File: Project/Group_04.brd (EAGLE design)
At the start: 71.4 x 57.1 mm, 29 parts, among them J1 POWER_JACKPTH_LOCK, U1 +12v

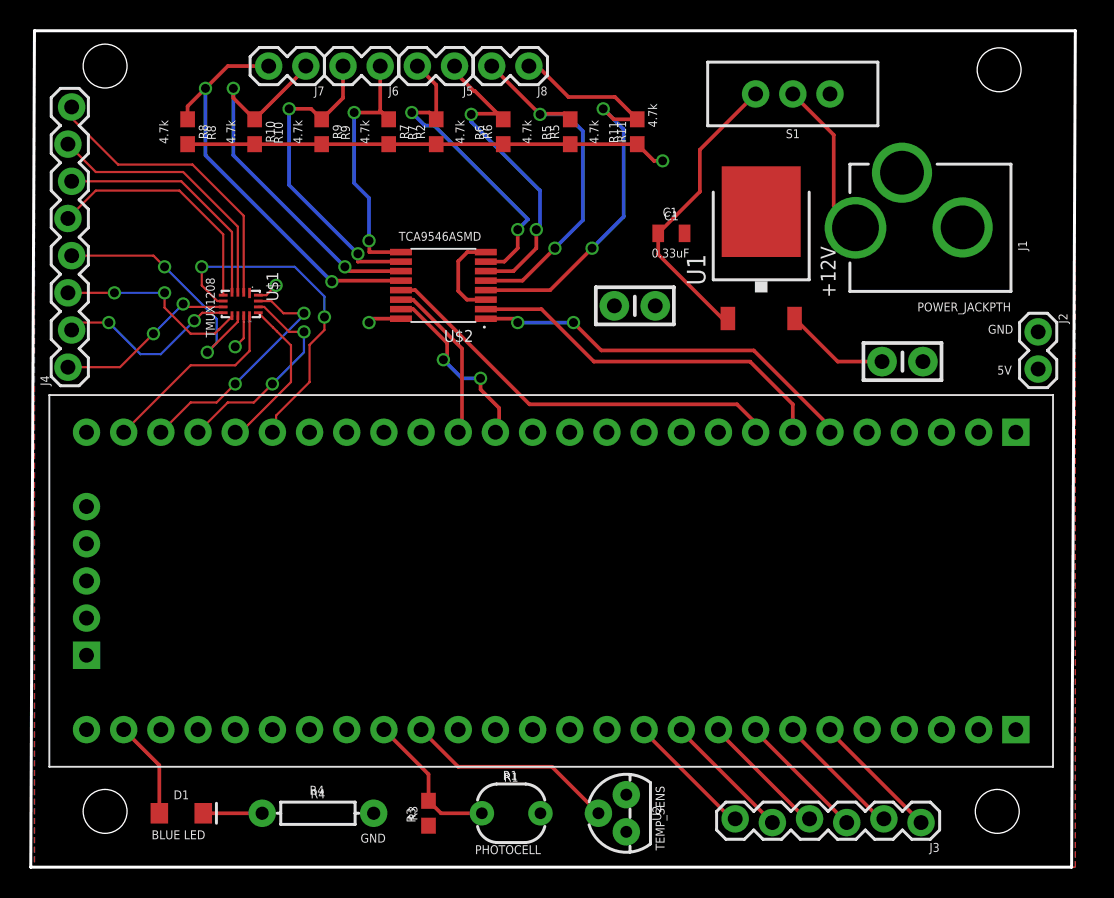
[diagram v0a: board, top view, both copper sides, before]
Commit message: fixed dimension
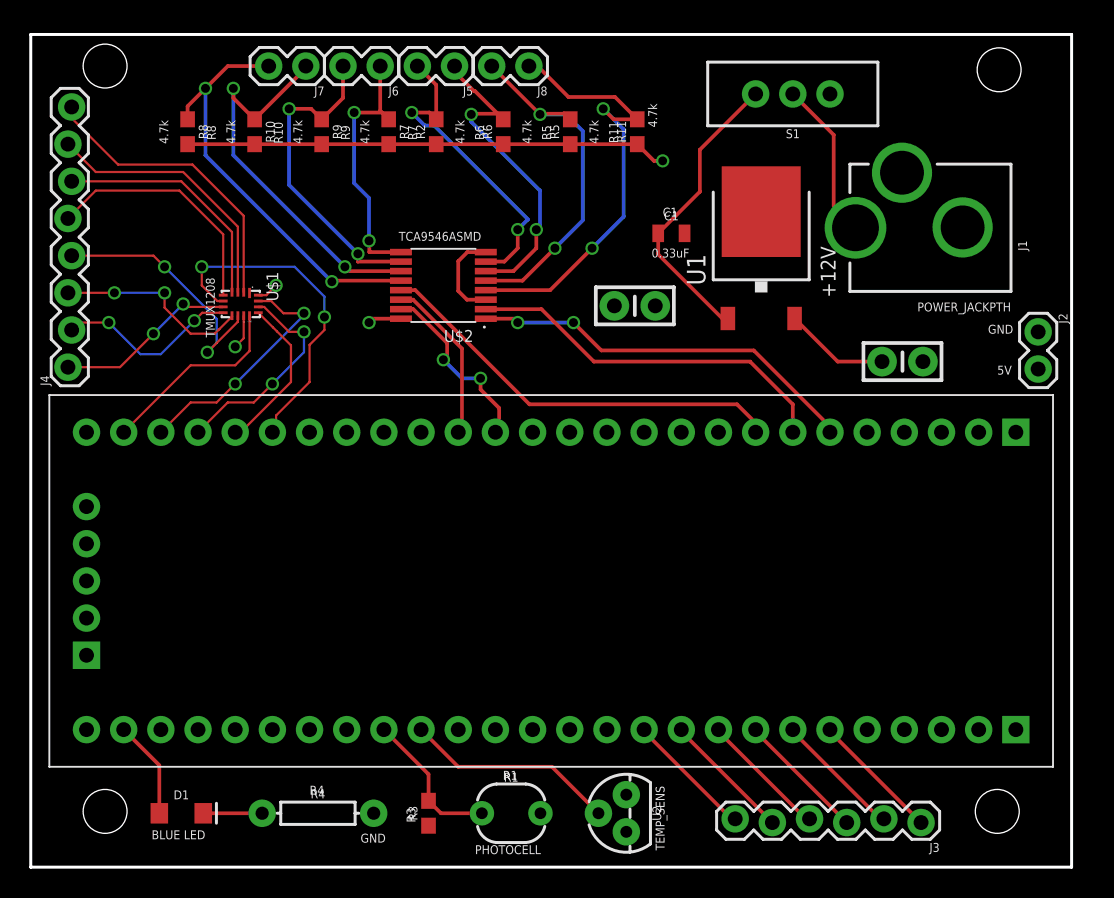
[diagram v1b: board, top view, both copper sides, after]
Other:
- board size 71.4 x 57.1 mm -> 71.1 x 56.9 mm
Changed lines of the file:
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@@
 <plain>
 <wire x1="0" y1="0" x2="71.12" y2="0" width="0.2032" layer="20"/>
-<wire x1="71.12" y1="0" x2="71.374" y2="57.15" width="0.2032" layer="20"/>
-<wire x1="71.374" y1="57.15" x2="0.254" y2="57.15" width="0.2032" layer="20"/>
-<wire x1="0.254" y1="57.15" x2="0" y2="0" width="0.2032" layer="20"/>
+<wire x1="71.12" y1="0" x2="71.12" y2="56.896" width="0.2032" layer="20"/>
+<wire x1="71.12" y1="56.896" x2="0" y2="56.896" width="0.2032" layer="20"/>
+<wire x1="0" y1="56.896" x2="0" y2="0" width="0.2032" layer="20"/>
 <hole x="5.08" y="3.81" drill="3"/>
 <hole x="66.04" y="3.81" drill="3"/>
@@
 <text x="14.478" y="37.211" size="0.1016" layer="21">5V</text>
 <dimension x1="0" y1="0" x2="71.12" y2="0" x3="35.56" y3="-3.81" textsize="1.778" layer="51" visible="yes"/>
-<dimension x1="0" y1="0" x2="0.254" y2="57.15" x3="-3.6829625" y3="28.59193125" textsize="1.778" layer="51" visible="yes"/>
+<dimension x1="0" y1="0" x2="0" y2="56.896" x3="-3.81" y3="28.448" textsize="1.778" layer="51" visible="yes"/>
 </plain>
 <attributes>
@@
 <contactref element="R3" pad="1"/>
 <polygon width="0.254" layer="1" isolate="0.3048">
-<vertex x="0.254" y="57.15"/>
-<vertex x="0.254" y="0"/>
-<vertex x="71.374" y="0"/>
-<vertex x="71.374" y="57.15"/>
+<vertex x="0" y="56.896"/>
+<vertex x="0" y="0"/>
+<vertex x="0" y="0"/>
+<vertex x="71.12" y="0"/>
+<vertex x="71.12" y="56.896"/>
 </polygon>
 <wire x1="31.094" y1="38.776" x2="29.804" y2="38.776" width="0.254" layer="1"/>
@@
 <wire x1="55.138" y1="34.544" x2="58.166" y2="34.544" width="0.254" layer="1"/>
 <polygon width="0.254" layer="16" isolate="0.3048">
-<vertex x="0.254" y="57.15"/>
-<vertex x="0.254" y="0"/>
-<vertex x="71.374" y="0"/>
-<vertex x="71.374" y="57.15"/>
+<vertex x="0" y="56.896"/>
+<vertex x="0" y="0"/>
+<vertex x="0" y="0"/>
+<vertex x="71.12" y="0"/>
+<vertex x="71.12" y="56.896"/>
 </polygon>
 <wire x1="25.294" y1="37.476" x2="23.379" y2="37.476" width="0.254" layer="1"/>

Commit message: Final version
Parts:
- moved J1 3.82 mm to (73.8, 45.1)
- moved U1 2.19 mm to (52.1, 42.7)
- moved C3 1.14 mm to (60.1, 35.6)
- moved C2 0.54 mm to (41.7, 38.0)
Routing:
- net 12V: track 20.3 -> 22.3 mm
- net 5V: track 46.3 -> 44.4 mm
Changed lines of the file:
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@@
 <text x="25.146" y="42.799" size="0.6096" layer="21">TCA9546ASMD</text>
 <text x="12.573" y="36.195" size="0.6096" layer="21" rot="R90">TMUX1208</text>
-<text x="53.975" y="42.418" size="1.016" layer="21" rot="R270">+12V</text>
+<text x="56.134" y="42.799" size="1.016" layer="21" rot="R270">+12V</text>
 <text x="9.398" y="49.41983125" size="0.6096" layer="21" rot="R90">4.7k</text>
 <text x="42.418" y="41.656" size="0.6096" layer="21">0.33uF</text>
 <text x="66.04" y="33.655" size="0.6096" layer="21">5V</text>
 <text x="65.405" y="36.449" size="0.6096" layer="21">GND</text>
-<text x="60.579" y="37.973" size="0.6096" layer="21">POWER_JACKPTH</text>
+<text x="60.833" y="39.624" size="0.6096" layer="21">POWER_JACKPTH</text>
 <text x="43.18" y="44.45" size="0.6096" layer="21">C1</text>
 <text x="13.977234375" y="49.41983125" size="0.6096" layer="21" rot="R90">4.7k</text>
@@
 <attribute name="VALUE" x="43.7729375" y="42.418" size="0.6096" layer="27" font="vector" ratio="20" align="top-center"/>
 </element>
-<element name="C2" library="SparkFun-Capacitors" package="CAP-PTH-SMALL-KIT" value="0.1uF" x="41.275" y="38.354" smashed="yes" rot="R180">
-<attribute name="PROD_ID" value="CAP-08370" x="-17.145" y="95.504" size="1.778" layer="27" rot="R180" display="off"/>
-</element>
-<element name="C3" library="SparkFun-Capacitors" package="CAP-PTH-SMALL-KIT" value="0.1uF" x="59.563" y="34.544" smashed="yes">
-<attribute name="PROD_ID" value="CAP-08370" x="124.333" y="-22.606" size="1.778" layer="27" display="off"/>
+<element name="C2" library="SparkFun-Capacitors" package="CAP-PTH-SMALL-KIT" value="0.1uF" x="41.656" y="37.973" smashed="yes" rot="R180">
+<attribute name="PROD_ID" value="CAP-08370" x="-16.764" y="95.123" size="1.778" layer="27" rot="R180" display="off"/>
+</element>
+<element name="C3" library="SparkFun-Capacitors" package="CAP-PTH-SMALL-KIT" value="0.1uF" x="60.071" y="35.56" smashed="yes">
+<attribute name="PROD_ID" value="CAP-08370" x="124.841" y="-21.59" size="1.778" layer="27" display="off"/>
 </element>
 <element name="D1" library="SparkFun-LED" package="LED-1206" value="BLUE" x="10.287" y="3.682953125" smashed="yes">
@@
 <attribute name="VALUE" x="10.287" y="2.730453125" size="0.6096" layer="27" font="vector" ratio="20" align="top-center"/>
 </element>
-<element name="J1" library="SparkFun-Connectors" package="POWER_JACK_PTH_LOCK" value="POWER_JACKPTH_LOCK" x="70.231" y="43.688" smashed="yes" rot="R90">
-<attribute name="NAME" x="68.072" y="42.1132" size="0.6096" layer="25" font="vector" ratio="20" rot="R90"/>
-<attribute name="PROD_ID" value="CONN-08197" x="98.171" y="64.008" size="1.778" layer="27" rot="R90" display="off"/>
-<attribute name="SF_ID" value="PRT-00119" x="98.171" y="64.008" size="1.778" layer="27" rot="R90" display="off"/>
-<attribute name="VALUE" x="69.088" y="41.783" size="0.6096" layer="27" font="vector" ratio="20" rot="R90"/>
+<element name="J1" library="SparkFun-Connectors" package="POWER_JACK_PTH_LOCK" value="POWER_JACKPTH_LOCK" x="73.787" y="45.085" smashed="yes" rot="R90">
+<attribute name="NAME" x="71.628" y="43.5102" size="0.6096" layer="25" font="vector" ratio="20" rot="R90"/>
+<attribute name="PROD_ID" value="CONN-08197" x="101.727" y="65.405" size="1.778" layer="27" rot="R90" display="off"/>
+<attribute name="SF_ID" value="PRT-00119" x="101.727" y="65.405" size="1.778" layer="27" rot="R90" display="off"/>
+<attribute name="VALUE" x="72.644" y="43.18" size="0.6096" layer="27" font="vector" ratio="20" rot="R90"/>
 </element>
 <element name="J2" library="SparkFun-Connectors" package="1X02" value="" x="68.834" y="36.576" smashed="yes" rot="R270">
@@
 </element>
 <element name="U$3" library="CY8KIT-059" package="CY8CKIT-059_TARGET" value="CY8CKIT-059_TARGET" x="36.83" y="20.828" smashed="yes"/>
-<element name="U1" library="SparkFun-IC-Power" package="TO-252" value="+12v" x="49.911" y="42.291" smashed="yes">
-<attribute name="NAME" x="46.101" y="39.751" size="1.27" layer="25" rot="R90"/>
-<attribute name="PROD_ID" value="VREG-12370" x="88.011" y="9.271" size="1.778" layer="27" display="off"/>
-<attribute name="VALUE" x="54.991" y="39.751" size="1.27" layer="27" rot="R90"/>
+<element name="U1" library="SparkFun-IC-Power" package="TO-252" value="+12v" x="52.07" y="42.672" smashed="yes">
+<attribute name="NAME" x="48.26" y="40.132" size="1.27" layer="25" rot="R90"/>
+<attribute name="PROD_ID" value="VREG-12370" x="90.17" y="9.652" size="1.778" layer="27" display="off"/>
+<attribute name="VALUE" x="57.15" y="40.132" size="1.27" layer="27" rot="R90"/>
 </element>
 <element name="U2" library="SparkFun-Sensors" package="TO-92" value="" x="40.6929125" y="3.682996875" smashed="yes" rot="R90">
@@
 <vertex x="0" y="56.896"/>
 <vertex x="0" y="0"/>
-<vertex x="0" y="0"/>
 <vertex x="71.12" y="0"/>
 <vertex x="71.12" y="56.896"/>
@@
 <contactref element="J1" pad="PWR"/>
 <contactref element="S1" pad="2"/>
-<wire x1="56.3532" y1="43.688" x2="54.864" y2="45.1772" width="0.254" layer="1"/>
-<wire x1="54.864" y1="50.038" x2="52.07" y2="52.832" width="0.254" layer="1"/>
-<wire x1="54.864" y1="45.1772" x2="54.864" y2="50.038" width="0.254" layer="1"/>
+<wire x1="59.9092" y1="45.085" x2="59.817" y2="45.085" width="0.254" layer="1"/>
+<wire x1="59.817" y1="45.085" x2="52.07" y2="52.832" width="0.254" layer="1"/>
 </signal>
 <signal name="12V">
@@
 <contactref element="C1" pad="1"/>
 <contactref element="U1" pad="1"/>
-<wire x1="47.631" y1="37.491" x2="47.25" y2="37.491" width="0.254" layer="1"/>
-<wire x1="47.25" y1="37.491" x2="42.8729375" y2="41.8680625" width="0.254" layer="1"/>
+<wire x1="49.79" y1="37.872" x2="46.869" y2="37.872" width="0.254" layer="1"/>
+<wire x1="46.869" y1="37.872" x2="42.8729375" y2="41.8680625" width="0.254" layer="1"/>
 <wire x1="42.8729375" y1="43.307" x2="42.8729375" y2="41.8680625" width="0.254" layer="1"/>
 <wire x1="45.72" y1="46.1540625" x2="42.8729375" y2="43.307" width="0.254" layer="1"/>
@@
 <wire x1="19.875946875" y1="49.3999375" x2="15.2967125" y2="49.3999375" width="0.254" layer="1"/>
 <wire x1="15.2967125" y1="49.3999375" x2="10.717478125" y2="49.3999375" width="0.254" layer="1"/>
-<wire x1="52.191" y1="37.491" x2="55.138" y2="34.544" width="0.254" layer="1"/>
-<wire x1="55.138" y1="34.544" x2="58.166" y2="34.544" width="0.254" layer="1"/>
+<wire x1="54.35" y1="37.872" x2="56.662" y2="35.56" width="0.254" layer="1"/>
+<wire x1="56.662" y1="35.56" x2="58.674" y2="35.56" width="0.254" layer="1"/>
 <polygon width="0.254" layer="16" isolate="0.3048">
 <vertex x="0" y="56.896"/>
 <vertex x="0" y="0"/>
-<vertex x="0" y="0"/>
 <vertex x="71.12" y="0"/>
